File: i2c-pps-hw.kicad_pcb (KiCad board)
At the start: 4 copper layers, 85 x 56 mm, 123 parts, among them J1 +5V, J2 Vout, J3 Digital I/O, Q1 SiR880BDP, Q2 SiR880BDP, Q3 SiR880BDP, Q4 SiR880BDP, Q5 SIS413DN, Q6 MMBT3904, Q7 MMBT3904, Q8 SIS413DN, U1 BQ25758S, U2 AP2210-3.3, U3 74AHC1G14

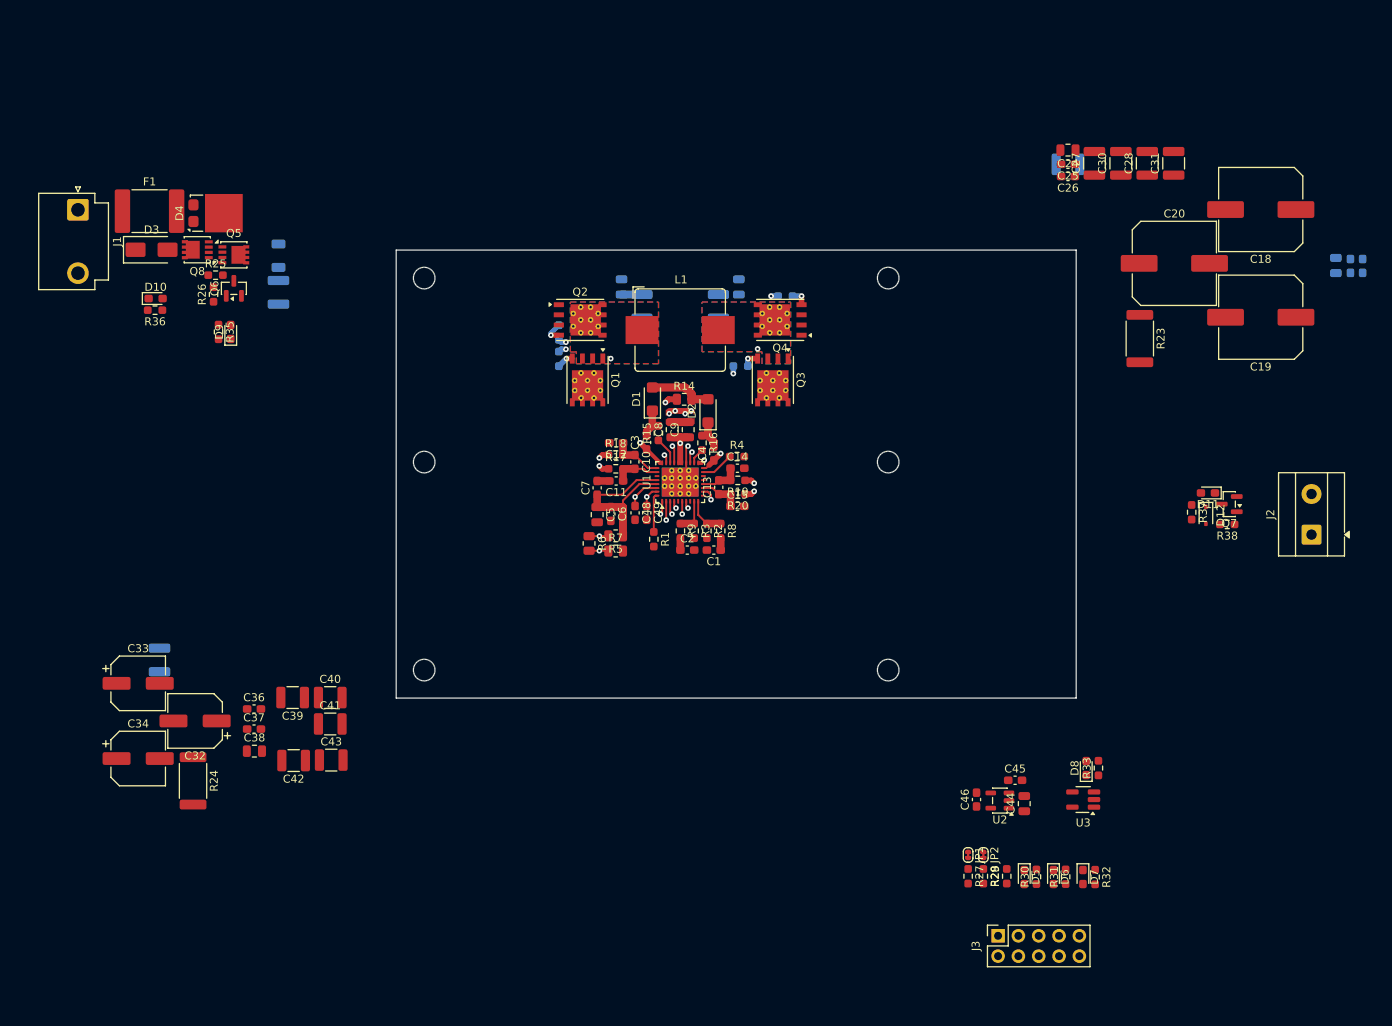
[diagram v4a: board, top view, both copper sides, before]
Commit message: Remove mounting and resize board
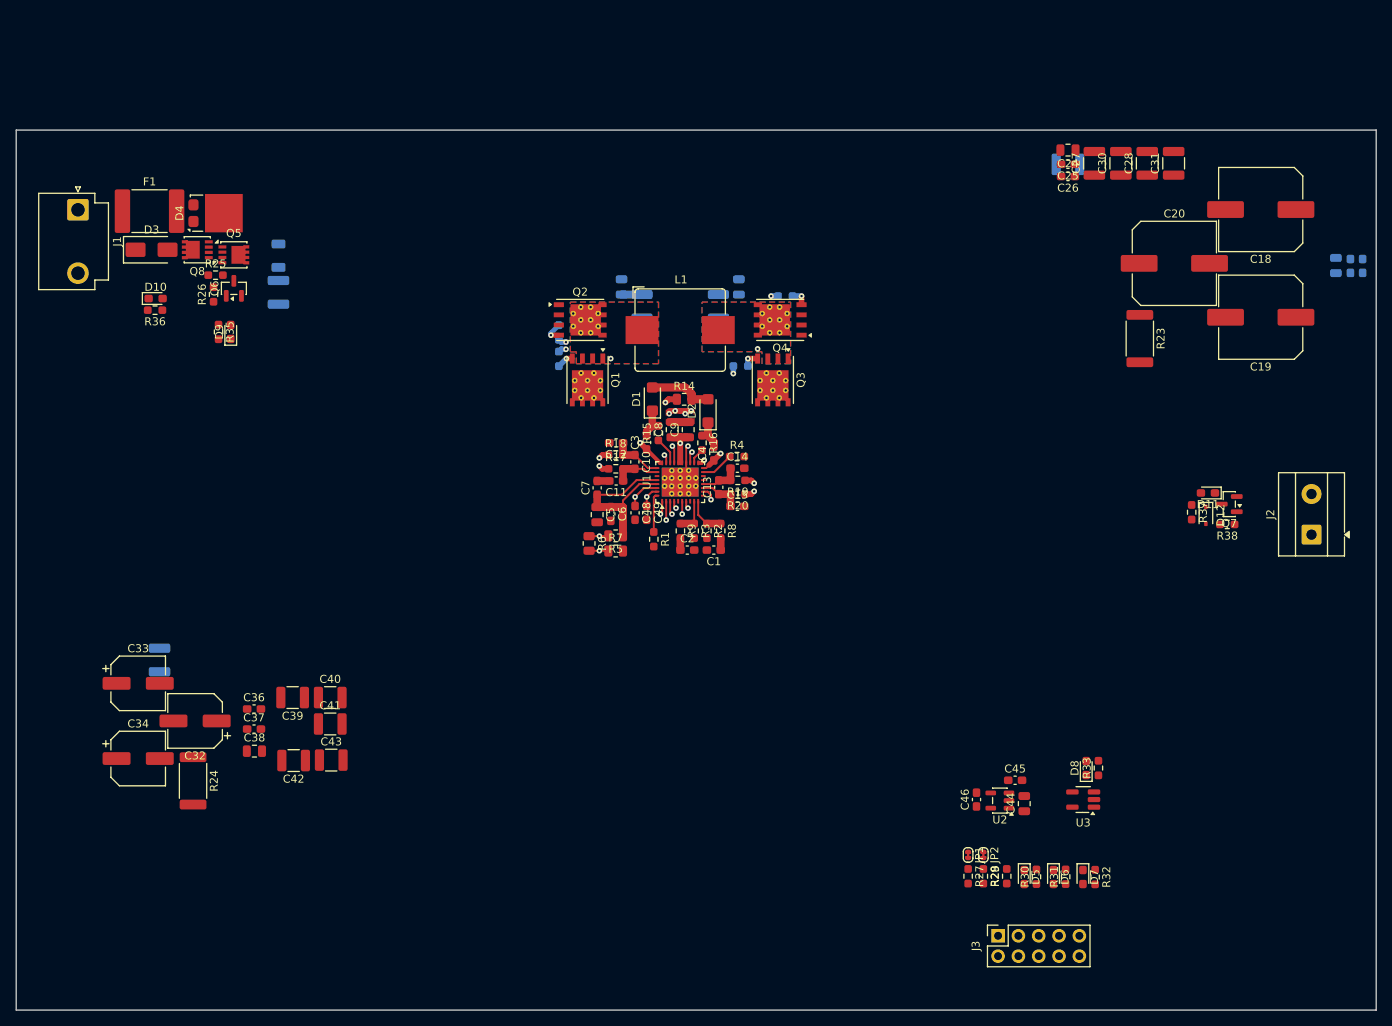
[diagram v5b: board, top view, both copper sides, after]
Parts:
- removed MH (x4), MHZ (x2): MountingHole_2.7mm_M2.5, MountingHole:MountingHole_2.7mm_M2.5
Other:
- board size 85 x 56 mm -> 170 x 110 mm

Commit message: Implement approximate component placement
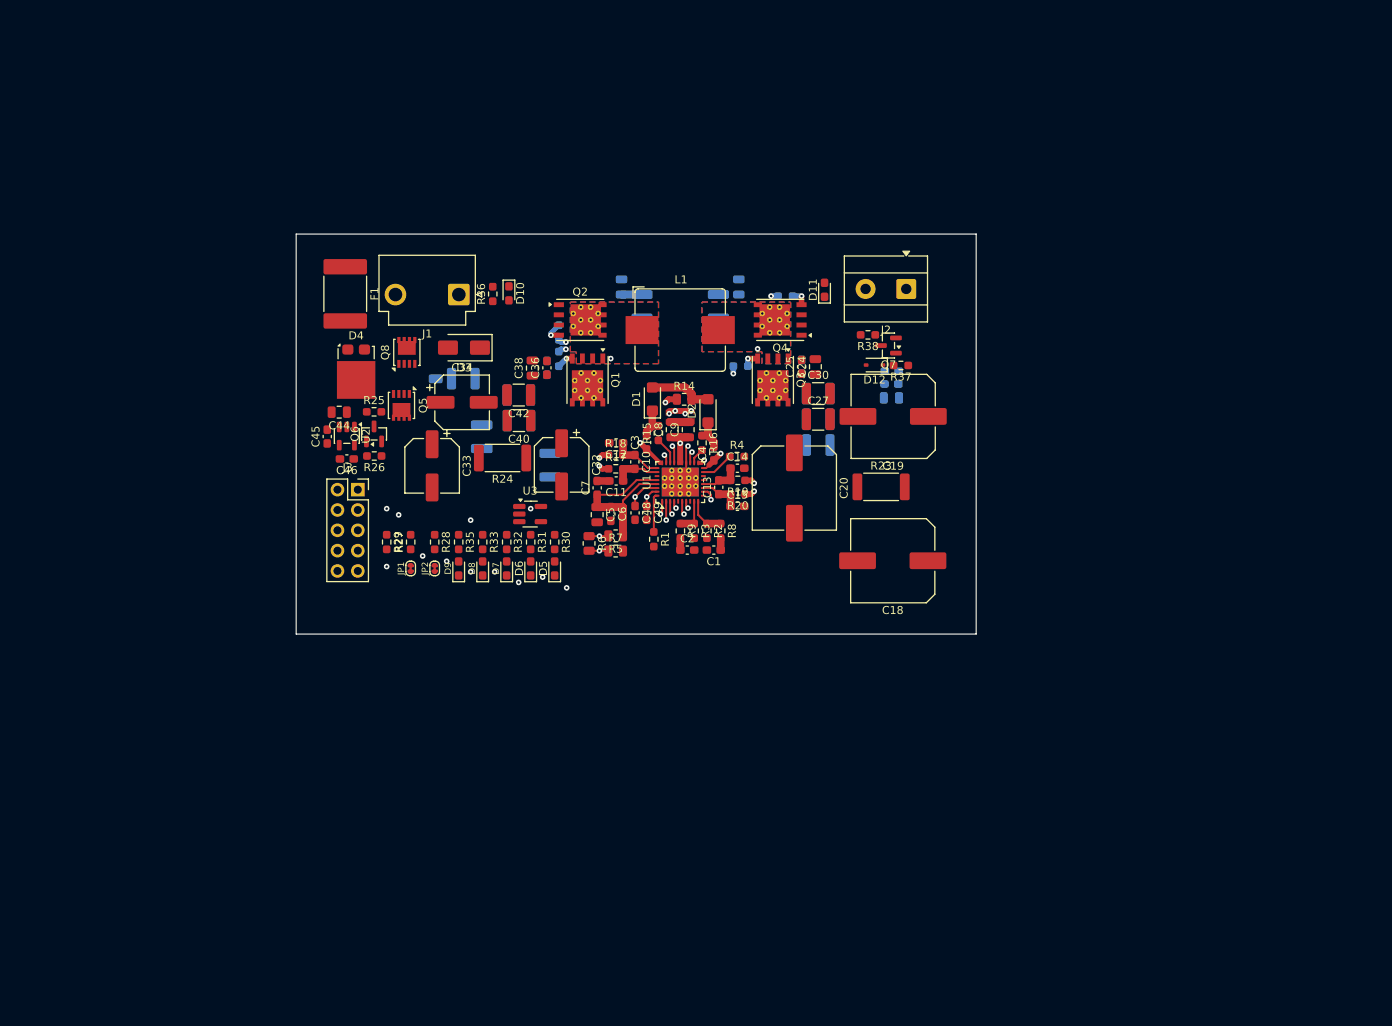
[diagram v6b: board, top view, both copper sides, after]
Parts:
- C26, C28, C31, C37, C39, C41, C43: moved to B.Cu
- moved C44 98.6 mm to (95.4, 100.3), turned to 180 degrees
- moved J3 97.5 mm to (97.7, 110.0), turned to 0 degrees
- moved C45 96.1 mm to (93.9, 103.3), turned to 90 degrees
- moved U2 93.5 mm to (96.3, 103.2), turned to -90 degrees
- moved C46 89.5 mm to (96.3, 106.1), turned to 180 degrees
- moved R29 88.0 mm to (101.3, 116.5), turned to -90 degrees
- moved R32 84.6 mm to (116.3, 116.5)
- moved R33 82.0 mm to (113.3, 116.5), turned to -90 degrees
- moved D7 81.7 mm to (116.3, 119.8), turned to 90 degrees
- moved R27 81.2 mm to (104.3, 116.5), turned to 90 degrees
- moved R28 80.3 mm to (107.3, 116.5)
- moved D8 79.5 mm to (113.3, 119.8)
- moved R31 78.9 mm to (119.3, 116.5), turned to -90 degrees
- moved JP1 78.3 mm to (104.3, 119.8), turned to 90 degrees
- moved U3 77.8 mm to (119.2, 113.0), turned to 0 degrees
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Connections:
- F1 pad 1: Net-(J1-Pin_1) -> /Master Switch/+5V
- J1 pad 1: Net-(J1-Pin_1) -> GND
- J1 pad 2: GND -> /Master Switch/+5V
- J3 pad 1: /Digital IO and Indication/+5V_Prot -> /Digital IO and Indication/3.3v
- J3 pad 2: /Digital IO and Indication/3.3v -> /Digital IO and Indication/+5V_Prot
- J3 pad 6: /Controller and Power Stage/SDA -> /Digital IO and Indication/CE
- J3 pad 7: /Digital IO and Indication/CE -> /Controller and Power Stage/SDA
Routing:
- net GND: track 9.06 -> 9.30 mm, vias 5 -> 7
- net /Controller and Power Stage/~{PG}: track 1.60 -> 1.69 mm, vias 1 -> 2
- net /Digital IO and Indication/EN: vias 0 -> 1
- net /Digital IO and Indication/CE: vias 0 -> 1
- net /Digital IO and Indication/3.3v: vias 0 -> 2
- net /Controller and Power Stage/~{INT}: vias 1 -> 2
- net /Controller and Power Stage/~{CE}: vias 1 -> 2
- net /Controller and Power Stage/STAT: vias 1 -> 2
- net /Controller and Power Stage/SDA: vias 1 -> 2
- net /Controller and Power Stage/SCL: vias 1 -> 2
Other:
- board size 170 x 110 mm -> 85 x 50 mm

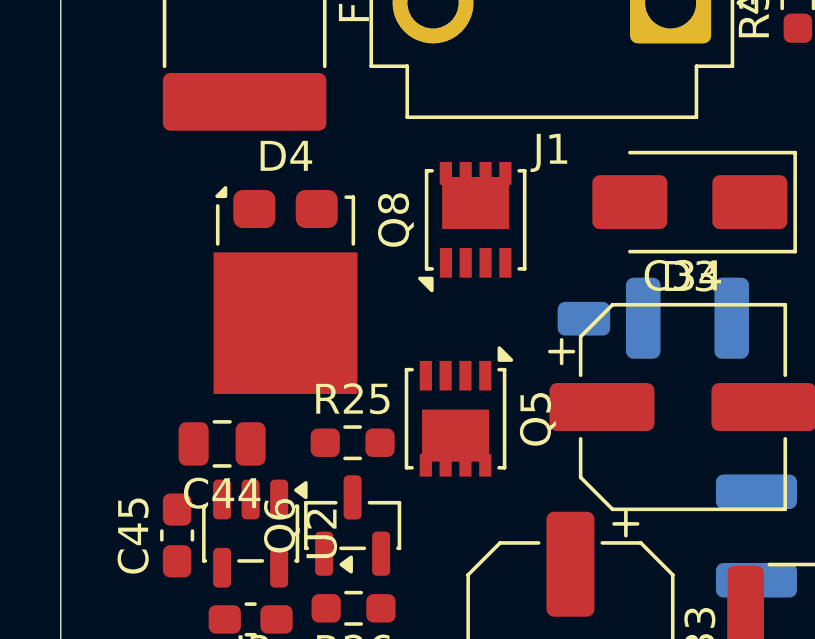
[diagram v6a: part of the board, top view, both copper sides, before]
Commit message: Add thermal vias to the master switch components
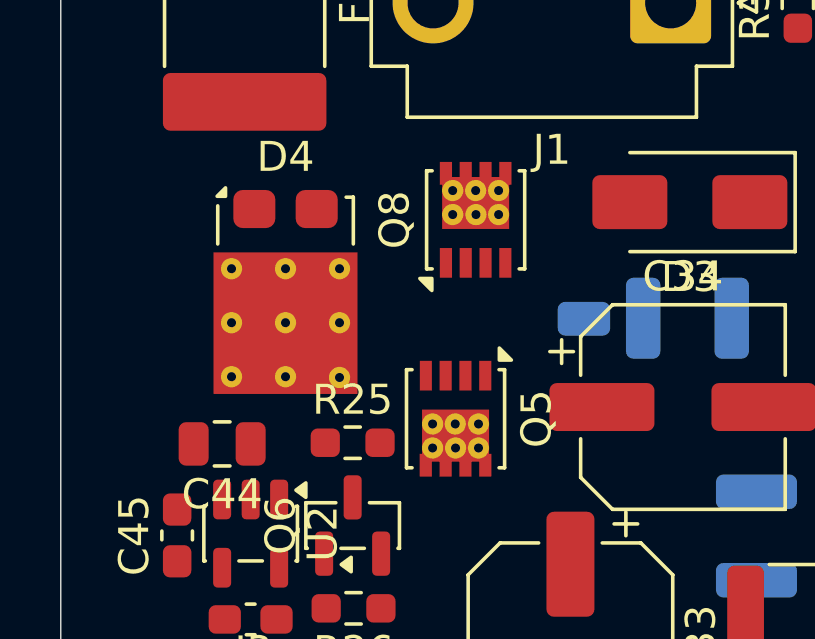
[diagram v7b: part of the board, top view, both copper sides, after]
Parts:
- D4: footprint Package_TO_SOT_SMD:TO-277A -> i2c-pps-hw:TO-277A_ThermalVias
- Q5, Q8: footprint Package_SO:Vishay_PowerPAK_1212-8_Single -> i2c-pps-hw:Vishay_PowerPAK_1212-8_Single_ThermalVias
